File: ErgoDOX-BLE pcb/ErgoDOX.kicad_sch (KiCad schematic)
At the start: 112 parts, among them J1 Conn_01x04, J2 Conn_01x02_Female, J4 Conn_01x02, J5 Conn_01x02, J6 6PIN, P1 USB_C_Plug_USB2.0, Q1 Q_NPN_BCE, SW0:10 SW0:3, SW0:11 SW0:2, SW0:12 SW0:1, SW0:7 SW0:6, SW0:8 SW0:5, SW0:9 SW0:4, SW1:10 SW1:3, SW1:11 SW1:2, SW1:12 SW1:1, SW1:13 SW1:0, SW1:9 SW1:4, SW2:10 SW2:3, SW2:11 SW2:2, SW2:12 SW2:1, SW2:13 SW2:0, SW2:7 SW2:6, SW2:8 SW2:5, SW2:9 SW2:4, SW3:10 SW3:3, SW3:11 SW3:2, SW3:12 SW3:1, SW3:13 SW3:0, SW3:8 SW3:5, SW3:9 SW3:4, SW4:10 SW4:3, SW4:11 SW4:2, SW4:12 SW4:1, SW4:13 SW4:0, SW4:7 SW4:6, SW4:8 SW4:5, SW4:9 SW4:4, SW5:10 SW5:3, SW5:11 SW5:2, SW5:12 SW5:1, SW5:13 SW5:0, SW5:7 SW5:6, SW5:8 SW5:5, SW5:9 SW5:4, U1 MCP23018, U2 MCP73831-2-OT, U3 TC1262-33

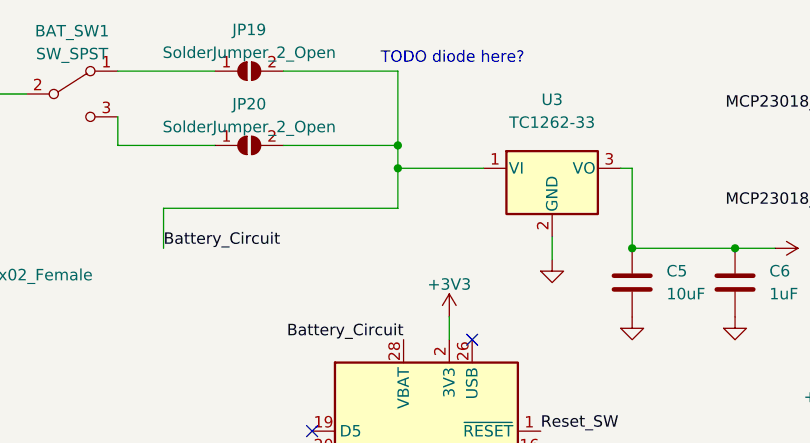
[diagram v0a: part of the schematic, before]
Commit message: Footprints for part of regulator circuit
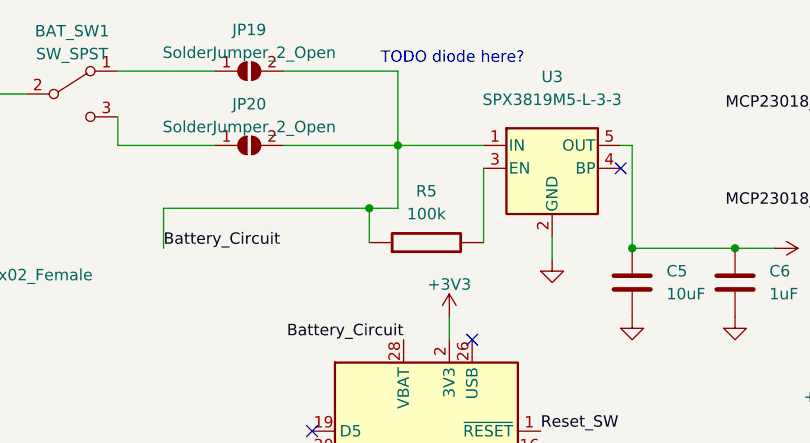
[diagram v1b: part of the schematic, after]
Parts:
- removed U3: TC1262-33, Package_TO_SOT_THT:TO-220-3_Vertical, symbol Regulator_Linear:TC1262-33
- added R5: 100k, Resistor_THT:R_Axial_DIN0207_L6.3mm_D2.5mm_P10.16mm_Horizontal, symbol component:RESISTOR
- added U3: SPX3819M5-L-3-3, Package_TO_SOT_SMD:SOT-23-5, symbol Regulator_Linear:SPX3819M5-L-3-3
- C5: footprint (none) -> Capacitor_SMD:C_0805_2012Metric_Pad1.18x1.45mm_HandSolder; manf# (none) -> CC0805ZKY5V6BB106
- C6: footprint (none) -> Capacitor_SMD:C_0402_1005Metric_Pad0.74x0.62mm_HandSolder; manf# (none) -> CL05A105KP5NNNC
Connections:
- net +3V3: now also U3.5 (OUT)
- net Battery_Circuit: now also R5.1, U3.1 (IN)
- net GND: now also U3.2 (GND)
- new net: R5.2, U3.3 (EN)
- no-connect marks 38 -> 39
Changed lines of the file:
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@@
   (junction (at 43.18 223.52) (diameter 0) (color 0 0 0 0)
   )
+  (junction (at 247.65 33.655) (diameter 0) (color 0 0 0 0)
+  )
   (junction (at 58.42 229.87) (diameter 0) (color 0 0 0 0)
   )
@@
   (junction (at 236.855 216.535) (diameter 0) (color 0 0 0 0)
   )
-  (junction (at 250.825 29.21) (diameter 0) (color 0 0 0 0)
-  )
   (junction (at 76.2 213.36) (diameter 0) (color 0 0 0 0)
   )
@@
   (no_connect (at 158.75 73.66))
   (no_connect (at 266.7 73.66))
+  (no_connect (at 275.59 29.21))
   (no_connect (at 277.495 224.155))
   (no_connect (at 277.495 196.85))
@@
     (stroke (width 0) (type default) (color 0 0 0 0))
   )
-  (wire (pts (xy 224.79 33.655) (xy 250.825 33.655))
+  (wire (pts (xy 224.79 33.655) (xy 247.65 33.655))
     (stroke (width 0) (type default) (color 0 0 0 0))
   )
@@
     (stroke (width 0) (type default) (color 0 0 0 0))
   )
-  (wire (pts (xy 275.59 29.21) (xy 276.86 29.21))
-    (stroke (width 0) (type default) (color 0 0 0 0))
-  )
   (wire (pts (xy 147.32 196.85) (xy 147.32 203.2))
     (stroke (width 0) (type default) (color 0 0 0 0))
@@
     (stroke (width 0) (type default) (color 0 0 0 0))
   )
-  (wire (pts (xy 250.825 26.67) (xy 250.825 29.21))
+  (wire (pts (xy 250.825 26.67) (xy 250.825 33.655))
     (stroke (width 0) (type default) (color 0 0 0 0))
   )
@@
     (stroke (width 0) (type default) (color 0 0 0 0))
   )
-  (wire (pts (xy 250.825 29.21) (xy 250.825 33.655))
-    (stroke (width 0) (type default) (color 0 0 0 0))
-  )
   (wire (pts (xy 73.66 172.72) (xy 73.66 170.18))
     (stroke (width 0) (type default) (color 0 0 0 0))
@@
     (stroke (width 0) (type default) (color 0 0 0 0))
   )
-  (wire (pts (xy 250.825 29.21) (xy 260.35 29.21))
-    (stroke (width 0) (type default) (color 0 0 0 0))
-  )
   (wire (pts (xy 96.52 205.74) (xy 96.52 222.25))
     (stroke (width 0) (type default) (color 0 0 0 0))
@@
     (stroke (width 0) (type default) (color 0 0 0 0))
   )
+  (wire (pts (xy 275.59 26.67) (xy 276.86 26.67))
+    (stroke (width 0) (type default) (color 0 0 0 0))
+  )
   (wire (pts (xy 129.54 229.87) (xy 129.54 236.22))
     (stroke (width 0) (type default) (color 0 0 0 0))
@@
     (stroke (width 0) (type default) (color 0 0 0 0))
   )
-  (wire (pts (xy 276.86 29.21) (xy 276.86 38.1))
+  (wire (pts (xy 276.86 26.67) (xy 276.86 38.1))
     (stroke (width 0) (type default) (color 0 0 0 0))
   )
@@
     (stroke (width 0) (type default) (color 0 0 0 0))
   )
+  (wire (pts (xy 247.65 33.655) (xy 247.65 37.465))
+    (stroke (width 0) (type default) (color 0 0 0 0))
+  )
+  (wire (pts (xy 247.65 33.655) (xy 250.825 33.655))
+    (stroke (width 0) (type default) (color 0 0 0 0))
+  )
   (wire (pts (xy 160.02 222.25) (xy 162.56 222.25))
     (stroke (width 0) (type default) (color 0 0 0 0))
@@
     (stroke (width 0) (type default) (color 0 0 0 0))
   )
+  (wire (pts (xy 260.35 29.21) (xy 260.35 37.465))
+    (stroke (width 0) (type default) (color 0 0 0 0))
+  )
   (wire (pts (xy 58.42 219.71) (xy 58.42 213.36))
     (stroke (width 0) (type default) (color 0 0 0 0))
@@
     (stroke (width 0) (type default) (color 0 0 0 0))
   )
+  (wire (pts (xy 250.825 26.67) (xy 260.35 26.67))
+    (stroke (width 0) (type default) (color 0 0 0 0))
+  )
   (wire (pts (xy 127 172.72) (xy 127 170.18))
     (stroke (width 0) (type default) (color 0 0 0 0))
@@
     (pin "1")
   )
+  (symbol (lib_id "component:RESISTOR") (at 254 37.465 90) (unit 1)
+    (in_bom yes) (on_board yes) (fields_autoplaced)
+    (property "Reference" "R5" (id 0) (at 254 31.75 90))
+    (property "Value" "100k" (id 1) (at 254 34.29 90))
+    (property "Footprint" "Resistor_THT:R_Axial_DIN0207_L6.3mm_D2.5mm_P10.16mm_Horizontal" (id 2) (at 254 37.465 0)
+      (effects (font (size 1.27 1.27)) hide)
+    )
+    (property "Datasheet" "https://www.seielect.com/Catalog/SEI-CF_CFM.pdf" (id 3) (at 254 37.465 0)
+      (effects (font (size 1.27 1.27)) hide)
+    )
+    (property "manf#" "CF18JT100K" (id 4) (at 254 37.465 90)
+      (effects (font (size 1.27 1.27)) hide)
+    )
+    (pin "1")
+    (pin "2")
+  )
   (symbol (lib_id "Jumper:SolderJumper_2_Open") (at 224.79 216.535 0) (unit 1)
     (in_bom yes) (on_board yes) (fields_autoplaced)
@@
     (pin "1")
   )
+  (symbol (lib_id "Regulator_Linear:SPX3819M5-L-3-3") (at 267.97 29.21 0) (unit 1)
+    (in_bom yes) (on_board yes) (fields_autoplaced)
+    (property "Reference" "U3" (id 0) (at 267.97 19.05 0))
+    (property "Value" "SPX3819M5-L-3-3" (id 1) (at 267.97 21.59 0))
+    (property "Footprint" "Package_TO_SOT_SMD:SOT-23-5" (id 2) (at 267.97 20.955 0)
+      (effects (font (size 1.27 1.27)) hide)
+    )
+    (property "Datasheet" "https://www.exar.com/content/document.ashx?id=22106&languageid=1033&type=Datasheet&partnumber=SPX3819&filename=SPX3819.pdf&part=SPX3819" (id 3) (at 267.97 29.21 0)
+      (effects (font (size 1.27 1.27)) hide)
+    )
+    (pin "1")
+    (pin "2")
+    (pin "3")
+    (pin "4")
+    (pin "5")
+  )
   (symbol (lib_id "Jumper:SolderJumper_2_Open") (at 209.55 247.65 0) (unit 1)
     (in_bom yes) (on_board yes)
@@
     (pin "2")
   )
-  (symbol (lib_id "Regulator_Linear:TC1262-33") (at 267.97 29.21 0) (unit 1)
-    (in_bom yes) (on_board yes) (fields_autoplaced)
-    (property "Reference" "U3" (id 0) (at 267.97 21.59 0))
-    (property "Value" "TC1262-33" (id 1) (at 267.97 24.13 0))
-    (property "Footprint" "Package_TO_SOT_THT:TO-220-3_Vertical" (id 2) (at 267.97 23.495 0)
-      (effects (font (size 1.27 1.27) italic) hide)
-    )
-    (property "Datasheet" "http://ww1.microchip.com/downloads/en/DeviceDoc/21373C.pdf" (id 3) (at 267.97 36.83 0)
-      (effects (font (size 1.27 1.27)) hide)
-    )
-    (pin "1")
-    (pin "2")
-    (pin "3")
-  )
   (symbol (lib_name "SolderJumper_2_Open_1") (lib_id "Jumper:SolderJumper_2_Open") (at 307.975 237.49 0) (unit 1)
     (in_bom yes) (on_board yes)
@@
       (effects (font (size 1.27 1.27)) (justify left))
     )
-    (property "Footprint" "" (id 2) (at 289.2552 45.72 0)
+    (property "Footprint" "Capacitor_SMD:C_0402_1005Metric_Pad0.74x0.62mm_HandSolder" (id 2) (at 289.2552 45.72 0)
+      (effects (font (size 1.27 1.27)) hide)
+    )
+    (property "Datasheet" "https://media.digikey.com/pdf/Data%20Sheets/Samsung%20PDFs/CL05A105KP5NNN_Specsheet%20(1).pdf" (id 3) (at 288.29 41.91 0)
       (effects (font (size 1.27 1.27)) hide)
     )
-    (property "Datasheet" "~" (id 3) (at 288.29 41.91 0)
+    (property "manf#" "CL05A105KP5NNNC" (id 4) (at 288.29 41.91 0)
       (effects (font (size 1.27 1.27)) hide)
     )
@@
       (effects (font (size 1.27 1.27)) (justify left))
     )
-    (property "Footprint" "" (id 2) (at 277.8252 45.72 0)
+    (property "Footprint" "Capacitor_SMD:C_0805_2012Metric_Pad1.18x1.45mm_HandSolder" (id 2) (at 277.8252 45.72 0)
       (effects (font (size 1.27 1.27)) hide)
     )
-    (property "Datasheet" "~" (id 3) (at 276.86 41.91 0)
+    (property "Datasheet" "https://www.yageo.com/upload/media/product/productsearch/datasheet/mlcc/UPY-GPHC_Y5V_6.3V-to-50V_11.pdf" (id 3) (at 276.86 41.91 0)
+      (effects (font (size 1.27 1.27)) hide)
+    )
+    (property "manf#" "CC0805ZKY5V6BB106" (id 4) (at 276.86 41.91 0)
       (effects (font (size 1.27 1.27)) hide)
     )
@@
     )
     (path "/d186e3cc-ae10-40d5-a0ba-8749430f37fb"
-      (reference "C5") (unit 1) (value "10uF") (footprint "")
+      (reference "C5") (unit 1) (value "10uF") (footprint "Capacitor_SMD:C_0805_2012Metric_Pad1.18x1.45mm_HandSolder")
     )
     (path "/ccf97a44-9fee-4d78-a51a-033d03dc2f8c"
-      (reference "C6") (unit 1) (value "1uF") (footprint "")
+      (reference "C6") (unit 1) (value "1uF") (footprint "Capacitor_SMD:C_0402_1005Metric_Pad0.74x0.62mm_HandSolder")
     )
     (path "/0a4aac90-e59d-4cda-b0a5-9767da3bc5a3"
@@
       (reference "R4") (unit 1) (value "10k") (footprint "")
     )
+    (path "/2261c62b-c1d7-43d6-829c-7da9168a6716"
+      (reference "R5") (unit 1) (value "100k") (footprint "Resistor_THT:R_Axial_DIN0207_L6.3mm_D2.5mm_P10.16mm_Horizontal")
+    )
     (path "/00000000-0000-0000-0000-00004f64e80f"
       (reference "RA1") (unit 1) (value "LEDa 145Ω") (footprint "ErgoDOX pcb:RESISTOR")
@@
       (reference "U2") (unit 1) (value "MCP73831-2-OT") (footprint "Package_TO_SOT_SMD:SOT-23-5")
     )
-    (path "/8f8b5bf3-6975-4127-8192-e4402542a8f2"
-      (reference "U3") (unit 1) (value "TC1262-33") (footprint "Package_TO_SOT_THT:TO-220-3_Vertical")
+    (path "/2da88624-fd71-4deb-a27b-4e3b8810dfb6"
+      (reference "U3") (unit 1) (value "SPX3819M5-L-3-3") (footprint "Package_TO_SOT_SMD:SOT-23-5")
     )
     (path "/541ff60d-8106-419f-8b31-7003c4d8f0bd"
